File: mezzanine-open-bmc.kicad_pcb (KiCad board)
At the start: 2 copper layers, 85 x 54 mm, 6 parts, among them P1 CONN_02X20, P2 CONN_02X20

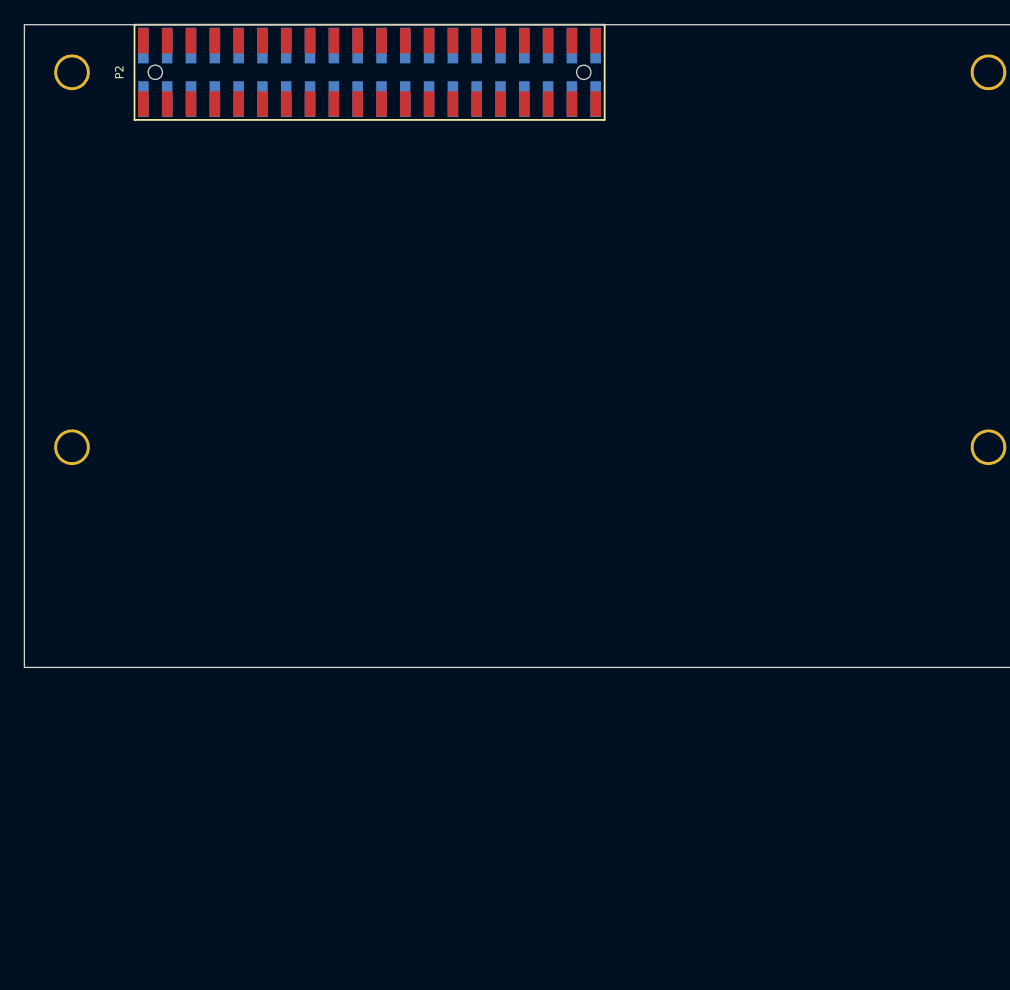
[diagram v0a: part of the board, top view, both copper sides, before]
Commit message: Assign More Footprints, Position Header
This commit add footprints to switches and the High Speed Connector (PCA9306).
In the PCB, the header pins are in the correct position now so that the two
stacking HiKey boards will be attatched one the same side and power ports
will be coming out of the same side.

Signed-off-by: Sophie Haynes <sophie.haynes@linaro.org>
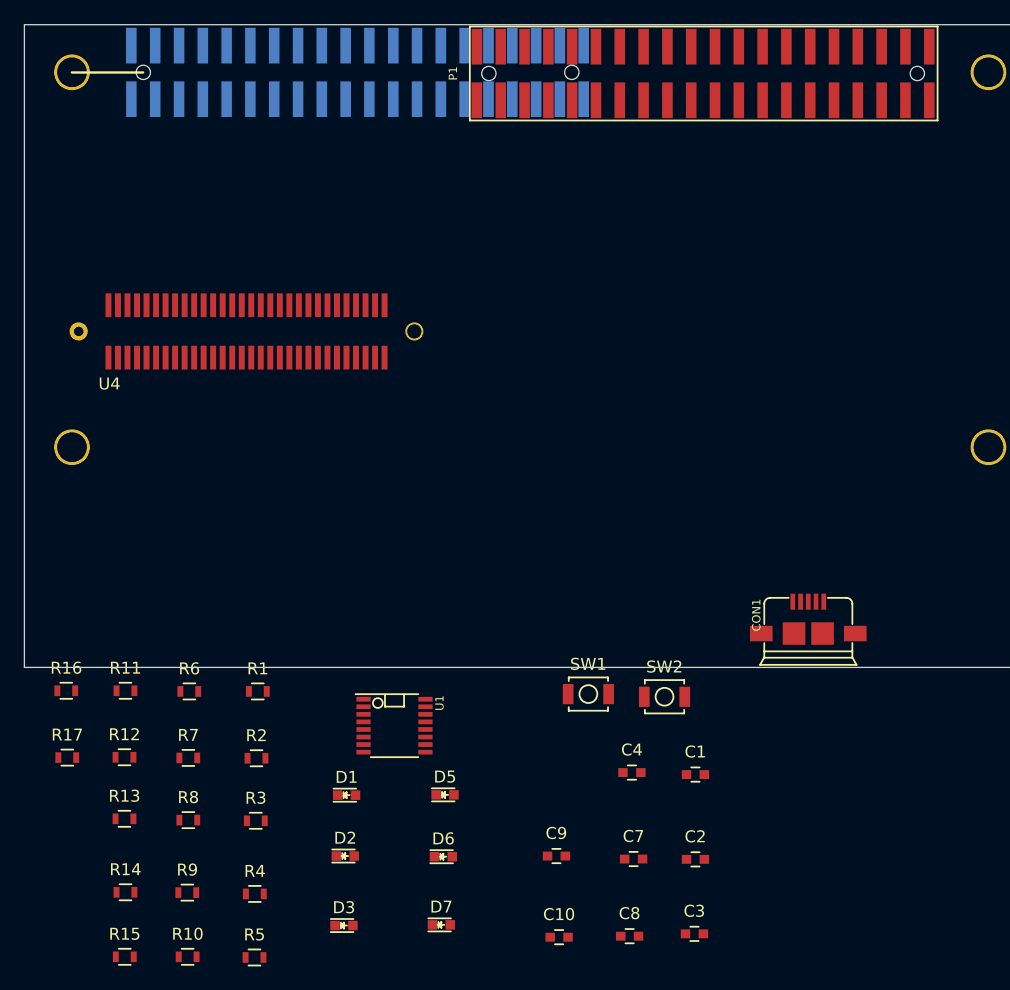
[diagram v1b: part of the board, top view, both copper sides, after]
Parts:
- added C1: 39pF, Capacitors_SMD:C_0603, F.Cu at (156.4, 163.0)
- added C10: 0.1n, Capacitors_SMD:C_0603, F.Cu at (144.9, 176.7)
- added C2: 39pF, Capacitors_SMD:C_0603, F.Cu at (156.4, 170.1)
- added C3: C_Small, Capacitors_SMD:C_0603, F.Cu at (156.3, 176.4)
- added C4: C_Small, Capacitors_SMD:C_0603, F.Cu at (151.0, 162.8)
- added C7: 0.47u, Capacitors_SMD:C_0603, F.Cu at (151.2, 170.1)
- added C8: 0.1u, Capacitors_SMD:C_0603, F.Cu at (150.8, 176.6)
- added C9: 0.1n, Capacitors_SMD:C_0603, F.Cu at (144.7, 169.8)
- added CON1: ~, 96boards:USB_MICRO_B_ST-USB-001E, F.Cu at (165.9, 152.7)
- added D1: Led_Small, LEDs:LED_0603, F.Cu at (127.1, 164.7)
- added D2: Led_Small, LEDs:LED_0603, F.Cu at (127.0, 169.8)
- added D3: Led_Small, LEDs:LED_0603, F.Cu at (126.8, 175.7)
- added D5: Led_Small, LEDs:LED_0603, F.Cu at (135.3, 164.7)
- added D6: Led_Small, LEDs:LED_0603, F.Cu at (135.2, 169.9)
- added D7: Led_Small, LEDs:LED_0603, F.Cu at (135.0, 175.6)
- added R1: 90Ω, Resistors_SMD:R_0603, F.Cu at (119.6, 156.0)
- added R10: 620R, Resistors_SMD:R_0603, F.Cu at (113.7, 178.3)
- added R11: 200k, Resistors_SMD:R_0603, F.Cu at (108.5, 156.0)
- added R12: 22R, Resistors_SMD:R_0603, F.Cu at (108.4, 161.5)
- added R13: 90Ω, Resistors_SMD:R_0603, F.Cu at (108.4, 166.7)
- added R14: 1k, Resistors_SMD:R_0603, F.Cu at (108.5, 172.9)
- added R15: 10k, Resistors_SMD:R_0603, F.Cu at (108.4, 178.3)
- added R16: 390R, Resistors_SMD:R_0603, F.Cu at (103.5, 156.0)
- added R17: 620R, Resistors_SMD:R_0603, F.Cu at (103.6, 161.6)
- added R2: 220R, Resistors_SMD:R_0603, F.Cu at (119.5, 161.6)
- added R3: 220R, Resistors_SMD:R_0603, F.Cu at (119.4, 166.9)
- added R4: 22R, Resistors_SMD:R_0603, F.Cu at (119.4, 173.0)
- added R5: 220R, Resistors_SMD:R_0603, F.Cu at (119.3, 178.4)
- added R6: 220R, Resistors_SMD:R_0603, F.Cu at (113.9, 156.0)
- added R7: 1k, Resistors_SMD:R_0603, F.Cu at (113.8, 161.6)
- added R8: 10k, Resistors_SMD:R_0603, F.Cu at (113.8, 166.8)
- added R9: 390R, Resistors_SMD:R_0603, F.Cu at (113.7, 172.9)
- added SW1: PWR, Buttons_Switches_SMD:SW_SPST_B3U-1000P, F.Cu at (147.4, 156.2)
- added SW2: RST, Buttons_Switches_SMD:SW_SPST_B3U-1000P, F.Cu at (153.8, 156.5)
- added U1: FT230XS, 96boards:SSOP-16_3.9x4.9mm_Pitch0.635mm_Seeed, F.Cu at (131.1, 158.9)
- added U4: PCA9306, 96boards:PCA9306, F.Cu at (107.1, 123.6)
- P1: moved to F.Cu
- P2: footprint 96boards:Socket_Strip_SMD_2x20_Pitch2mm -> 96boards:Pin_Header_SMD_2x20_Pitch2mm; moved to B.Cu
- moved P1 28.1 mm to (138.0, 103.1), turned to 90 degrees
- moved P2 1.01 mm to (109.0, 105.0), turned to 270 degrees
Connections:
- net GND renamed +3V3
- P1 pad 11: UART1_TX -> UART0_RX_BMC
- P1 pad 13: UART1_RX -> UART0_TX_BMC
- P1 pad 4: PWR_BTN_N -> GPIO_C_BMC
- P1 pad 6: RST_BTN_N -> GPIO_D_BMC
- P2 pad 10: SPIO_DIN -> SPIO_DIN_BMC
- P2 pad 11: UART1_TX -> UART1_TX_BMC
- P2 pad 12: SPIO_CS -> SPIO_CS_BMC
- P2 pad 13: UART1_RX -> UART1_RX_BMC
- P2 pad 14: SPIO_DOUT -> SPIO_DOUT_BMC
- P2 pad 15: I2C0_SCL -> I2C0_SCL_BMC
- P2 pad 16: PCM_FS -> PCM_FS_BMC
- P2 pad 17: I2C0_SDA -> I2C0_SDA_BMC
- P2 pad 18: PCM_CLK -> PCM_CLK_BMC
- P2 pad 19: I2C1_SCL -> I2C1_SCL_BMC
- P2 pad 20: PCM_DO -> PCM_DO_BMC
- P2 pad 21: I2C1_SDA -> I2C1_SDA_BMC
- P2 pad 22: PCM_DI -> PCM_DI_BMC
- P2 pad 25: GPIO_C -> GPIO_C_BMC
- P2 pad 26: GPIO_D -> GPIO_D_BMC
- P2 pad 27: GPIO_E -> GPIO_E_BMC
- P2 pad 28: GPIO_F -> GPIO_F_BMC
- P2 pad 29: GPIO_G -> GPIO_G_BMC
- P2 pad 3: UART0_CTS -> UART0_CTS_BMC
- P2 pad 30: GPIO_H -> GPIO_H_BMC
- P2 pad 31: GPIO_I -> GPIO_I_BMC
- P2 pad 32: GPIO_J -> GPIO_J_BMC
- P2 pad 33: GPIO_K -> GPIO_K_BMC
- P2 pad 34: GPIO_L -> GPIO_L_BMC
- P2 pad 36: SYS_DCIN -> SYS_DCIN_BMC
- P2 pad 38: SYS_DCIN -> SYS_DCIN_BMC
- P2 pad 4: PWR_BTN_N -> PWR_BTN_BMC
- P2 pad 5: UART0_TX -> UART0_TX_BMC
- P2 pad 6: RST_BTN_N -> RST_BTN_BMC
- P2 pad 7: UART0_RX -> UART0_RX_BMC
- P2 pad 8: SPIO_SCL -> SPIO_SCL_BMC
- P2 pad 9: UART0_RTS -> UART0_RTS_BMC

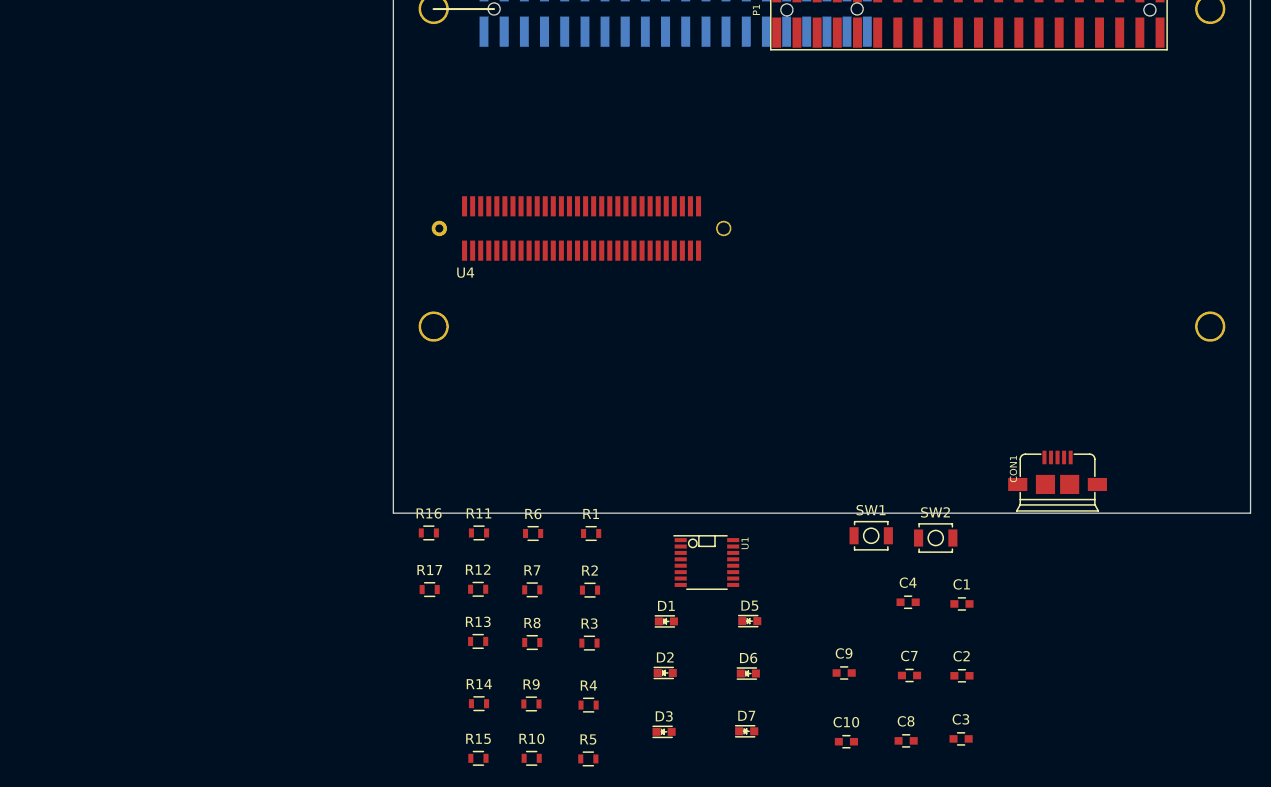
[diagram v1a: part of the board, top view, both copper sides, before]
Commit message: Group Components on PCB
Components have been grouped in the PCB to make it tidier and make positioning
easier.
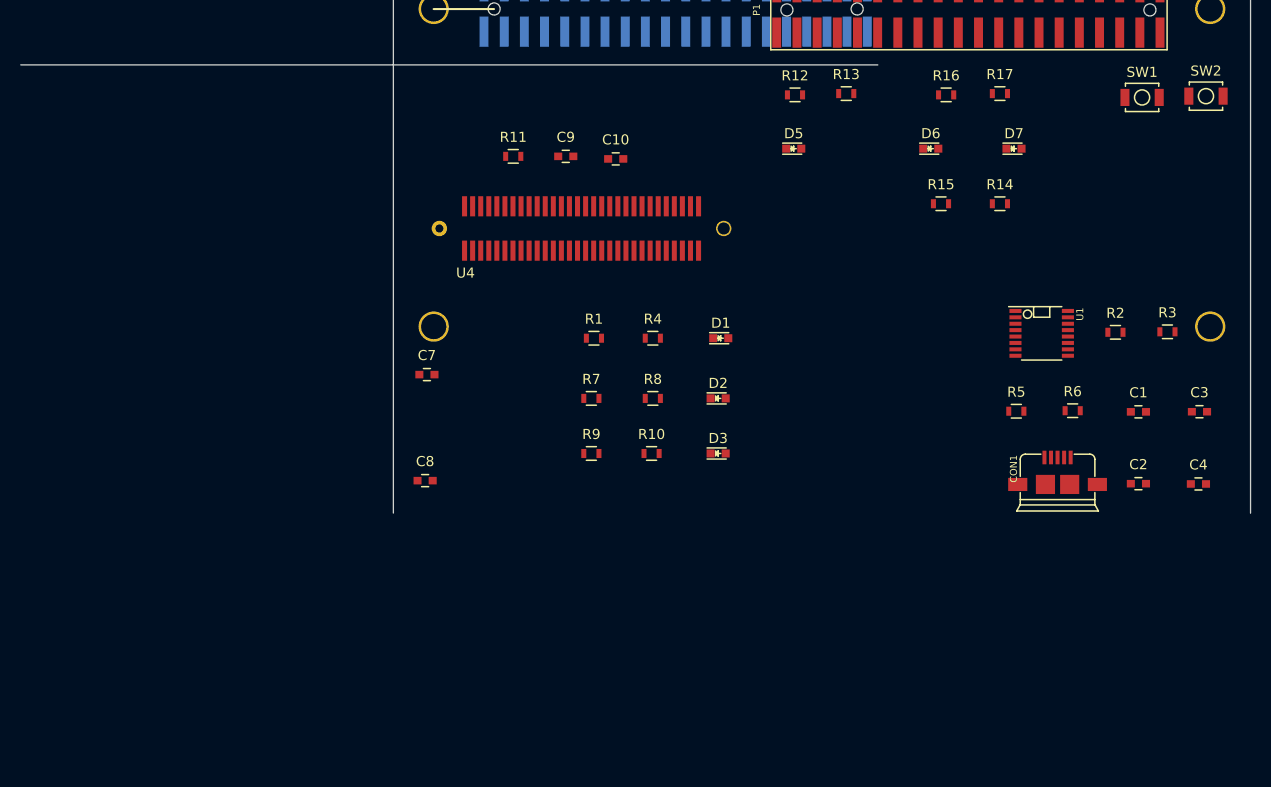
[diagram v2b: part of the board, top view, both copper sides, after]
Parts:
- moved R17 74.9 mm to (160.1, 112.4)
- moved R15 71.6 mm to (154.3, 123.3)
- moved R14 71.6 mm to (160.1, 123.3)
- moved R16 67.2 mm to (154.8, 112.5)
- moved R13 65.4 mm to (144.9, 112.4)
- moved R3 65.1 mm to (176.8, 136.0)
- moved D7 63.6 mm to (161.5, 117.9)
- moved C10 62.2 mm to (122.0, 118.9)
- moved R12 58.2 mm to (139.8, 112.5)
- moved C9 58.2 mm to (117.1, 118.6)
- moved R2 58.0 mm to (171.6, 136.1)
- moved C7 56.4 mm to (103.3, 140.3)
- moved D6 55.1 mm to (153.3, 117.9)
- moved R6 54.9 mm to (167.4, 143.8)
- moved R5 54.7 mm to (161.8, 143.9)
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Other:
- board size 85 x 54 mm -> 122 x 54 mm
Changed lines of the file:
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@@
   )
   (module Capacitors_SMD:C_0603 (layer F.Cu)
-    (at 156.38038 163.00216)
+    (at 173.88098 143.95216)
     (descr "Capacitor SMD 0603, reflow soldering, AVX (see smccp.pdf)")
     (tags "capacitor 0603")
@@
   )
   (module Capacitors_SMD:C_0603 (layer F.Cu)
-    (at 156.38038 170.12686)
+    (at 173.88098 151.07686)
     (descr "Capacitor SMD 0603, reflow soldering, AVX (see smccp.pdf)")
     (tags "capacitor 0603")
@@
   )
   (module Capacitors_SMD:C_0603 (layer F.Cu)
-    (at 156.29656 176.38542)
+    (at 179.9338 143.942)
     (descr "Capacitor SMD 0603, reflow soldering, AVX (see smccp.pdf)")
     (tags "capacitor 0603")
@@
   )
   (module Capacitors_SMD:C_0603 (layer F.Cu)
-    (at 151.04384 162.83452)
+    (at 179.8322 151.1048)
     (descr "Capacitor SMD 0603, reflow soldering, AVX (see smccp.pdf)")
     (tags "capacitor 0603")
@@
   )
   (module Capacitors_SMD:C_0603 (layer F.Cu)
-    (at 151.18354 170.09892)
+    (at 103.3274 140.259)
     (descr "Capacitor SMD 0603, reflow soldering, AVX (see smccp.pdf)")
     (tags "capacitor 0603")
@@
   )
   (module Capacitors_SMD:C_0603 (layer F.Cu)
-    (at 150.84826 176.581)
+    (at 103.1496 150.7746)
     (descr "Capacitor SMD 0603, reflow soldering, AVX (see smccp.pdf)")
     (tags "capacitor 0603")
@@
   )
   (module Capacitors_SMD:C_0603 (layer F.Cu)
-    (at 144.70146 169.84746)
+    (at 117.0942 118.6182)
     (descr "Capacitor SMD 0603, reflow soldering, AVX (see smccp.pdf)")
     (tags "capacitor 0603")
@@
   )
   (module Capacitors_SMD:C_0603 (layer F.Cu)
-    (at 144.92498 176.66482)
+    (at 122.0472 118.8722)
     (descr "Capacitor SMD 0603, reflow soldering, AVX (see smccp.pdf)")
     (tags "capacitor 0603")
@@
   )
   (module LEDs:LED_0603 (layer F.Cu)
-    (at 127.07132 164.73444)
+    (at 132.4612 136.6522)
     (descr "LED 0603 smd package")
     (tags "LED led 0603 SMD smd SMT smt smdled SMDLED smtled SMTLED")
@@
   )
   (module LEDs:LED_0603 (layer F.Cu)
-    (at 126.95956 169.84746)
+    (at 132.2072 142.6212)
     (descr "LED 0603 smd package")
     (tags "LED led 0603 SMD smd SMT smt smdled SMDLED smtled SMTLED")
@@
   )
   (module LEDs:LED_0603 (layer F.Cu)
-    (at 126.8478 175.68692)
+    (at 132.2072 148.0822)
     (descr "LED 0603 smd package")
     (tags "LED led 0603 SMD smd SMT smt smdled SMDLED smtled SMTLED")
@@
   )
   (module LEDs:LED_0603 (layer F.Cu)
-    (at 135.34156 164.7065)
+    (at 139.7002 117.8562)
     (descr "LED 0603 smd package")
     (tags "LED led 0603 SMD smd SMT smt smdled SMDLED smtled SMTLED")
@@
   )
   (module LEDs:LED_0603 (layer F.Cu)
-    (at 135.20186 169.90334)
+    (at 153.2892 117.8562)
     (descr "LED 0603 smd package")
     (tags "LED led 0603 SMD smd SMT smt smdled SMDLED smtled SMTLED")
@@
   )
   (module LEDs:LED_0603 (layer F.Cu)
-    (at 135.03422 175.63104)
+    (at 161.5442 117.8562)
     (descr "LED 0603 smd package")
     (tags "LED led 0603 SMD smd SMT smt smdled SMDLED smtled SMTLED")
@@
   )
   (module Resistors_SMD:R_0603 (layer F.Cu)
-    (at 119.61134 156.01716)
+    (at 119.8882 136.6522)
     (descr "Resistor SMD 0603, reflow soldering, Vishay (see dcrcw.pdf)")
     (tags "resistor 0603")
@@
   )
   (module Resistors_SMD:R_0603 (layer F.Cu)
-    (at 119.49958 161.6331)
+    (at 171.6026 136.068)
     (descr "Resistor SMD 0603, reflow soldering, Vishay (see dcrcw.pdf)")
     (tags "resistor 0603")
@@
   )
   (module Resistors_SMD:R_0603 (layer F.Cu)
-    (at 119.4437 166.88582)
+    (at 176.7588 136.0172)
     (descr "Resistor SMD 0603, reflow soldering, Vishay (see dcrcw.pdf)")
     (tags "resistor 0603")
@@
   )
   (module Resistors_SMD:R_0603 (layer F.Cu)
-    (at 119.35988 173.03262)
+    (at 125.7302 136.6522)
     (descr "Resistor SMD 0603, reflow soldering, Vishay (see dcrcw.pdf)")
     (tags "resistor 0603")
@@
   )
   (module Resistors_SMD:R_0603 (layer F.Cu)
-    (at 119.33194 178.36916)
+    (at 161.7728 143.8912)
     (descr "Resistor SMD 0603, reflow soldering, Vishay (see dcrcw.pdf)")
     (tags "resistor 0603")
@@
   )
   (module Resistors_SMD:R_0603 (layer F.Cu)
-    (at 113.8557 156.01716)
+    (at 167.3608 143.8404)
     (descr "Resistor SMD 0603, reflow soldering, Vishay (see dcrcw.pdf)")
     (tags "resistor 0603")
@@
   )
   (module Resistors_SMD:R_0603 (layer F.Cu)
-    (at 113.77188 161.60516)
+    (at 119.6342 142.6212)
     (descr "Resistor SMD 0603, reflow soldering, Vishay (see dcrcw.pdf)")
     (tags "resistor 0603")
@@
   )
   (module Resistors_SMD:R_0603 (layer F.Cu)
-    (at 113.77188 166.82994)
+    (at 125.7302 142.6212)
     (descr "Resistor SMD 0603, reflow soldering, Vishay (see dcrcw.pdf)")
     (tags "resistor 0603")
@@
   )
   (module Resistors_SMD:R_0603 (layer F.Cu)
-    (at 113.68806 172.92086)
+    (at 119.6342 148.0822)
     (descr "Resistor SMD 0603, reflow soldering, Vishay (see dcrcw.pdf)")
     (tags "resistor 0603")
@@
   )
   (module Resistors_SMD:R_0603 (layer F.Cu)
-    (at 113.716 178.31328)
+    (at 125.6032 148.0822)
     (descr "Resistor SMD 0603, reflow soldering, Vishay (see dcrcw.pdf)")
     (tags "resistor 0603")
@@
   )
   (module Resistors_SMD:R_0603 (layer F.Cu)
-    (at 108.49122 155.96128)
+    (at 111.8872 118.6182)
     (descr "Resistor SMD 0603, reflow soldering, Vishay (see dcrcw.pdf)")
     (tags "resistor 0603")
@@
   )
   (module Resistors_SMD:R_0603 (layer F.Cu)
-    (at 108.4074 161.54928)
+    (at 139.8272 112.5222)
     (descr "Resistor SMD 0603, reflow soldering, Vishay (see dcrcw.pdf)")
     (tags "resistor 0603")
@@
   )
   (module Resistors_SMD:R_0603 (layer F.Cu)
-    (at 108.4074 166.71818)
+    (at 144.9072 112.3952)
     (descr "Resistor SMD 0603, reflow soldering, Vishay (see dcrcw.pdf)")
     (tags "resistor 0603")
@@
   )
   (module Resistors_SMD:R_0603 (layer F.Cu)
-    (at 108.49122 172.89292)
+    (at 160.1472 123.3172)
     (descr "Resistor SMD 0603, reflow soldering, Vishay (see dcrcw.pdf)")
     (tags "resistor 0603")
@@
   )
   (module Resistors_SMD:R_0603 (layer F.Cu)
-    (at 108.43534 178.31328)
+    (at 154.3052 123.3172)
     (descr "Resistor SMD 0603, reflow soldering, Vishay (see dcrcw.pdf)")
     (tags "resistor 0603")
@@
   )
   (module Resistors_SMD:R_0603 (layer F.Cu)
-    (at 103.5179 155.96128)
+    (at 154.8132 112.5222)
     (descr "Resistor SMD 0603, reflow soldering, Vishay (see dcrcw.pdf)")
     (tags "resistor 0603")
@@
   )
   (module Resistors_SMD:R_0603 (layer F.Cu)
-    (at 103.60172 161.57722)
+    (at 160.1472 112.3952)
     (descr "Resistor SMD 0603, reflow soldering, Vishay (see dcrcw.pdf)")
     (tags "resistor 0603")
@@
   )
   (module Buttons_Switches_SMD:SW_SPST_B3U-1000P (layer F.Cu)
-    (at 147.3837 156.24068)
+    (at 174.2442 112.7762)
     (descr "Ultra-small-sized Tactile Switch with High Contact Reliability, Top-actuated Model, without Ground Terminal, without Boss")
     (tags "Tactile Switch")
@@
   )
   (module Buttons_Switches_SMD:SW_SPST_B3U-1000P (layer F.Cu)
-    (at 153.78196 156.4642)
+    (at 180.57896 112.6492)
     (descr "Ultra-small-sized Tactile Switch with High Contact Reliability, Top-actuated Model, without Ground Terminal, without Boss")
     (tags "Tactile Switch")
@@
   )
   (module 96boards:SSOP-16_3.9x4.9mm_Pitch0.635mm_Seeed (layer F.Cu)
-    (at 131.09468 158.89498)
+    (at 164.2874 136.1696)
     (descr "SSOP16: plastic shrink small outline package; 16 leads; body width 3.9 mm; lead pitch 0.635; (see NXP SSOP-TSSOP-VSO-REFLOW.pdf and sot519-1_po.pdf)")
     (tags "SSOP 0.635")
@@
     (arrow2b (pts (xy 90 154) (xy 89.413579 152.873496)))
   )
-  (gr_line (start 100 154) (end 184.999492 154) (angle 90) (layer Edge.Cuts) (width 0.1))
+  (gr_line (start 63.043 109.55) (end 148.042492 109.55) (angle 90) (layer Edge.Cuts) (width 0.1))
   (gr_line (start 184.999492 100) (end 184.999492 154) (angle 90) (layer Edge.Cuts) (width 0.1))
   (gr_line (start 100 154) (end 100 100) (angle 90) (layer Edge.Cuts) (width 0.1))
